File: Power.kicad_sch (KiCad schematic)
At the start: 45 parts, among them J1 Conn_01x02, J7 Conn_01x02, J8 Conn_01x02, U3 TLV75533PDRV, U6 LMR51450FNDRR, U7 LMR51450FNDRR, U8 TPS259472LRPWR, U9 NSR0340HT1G

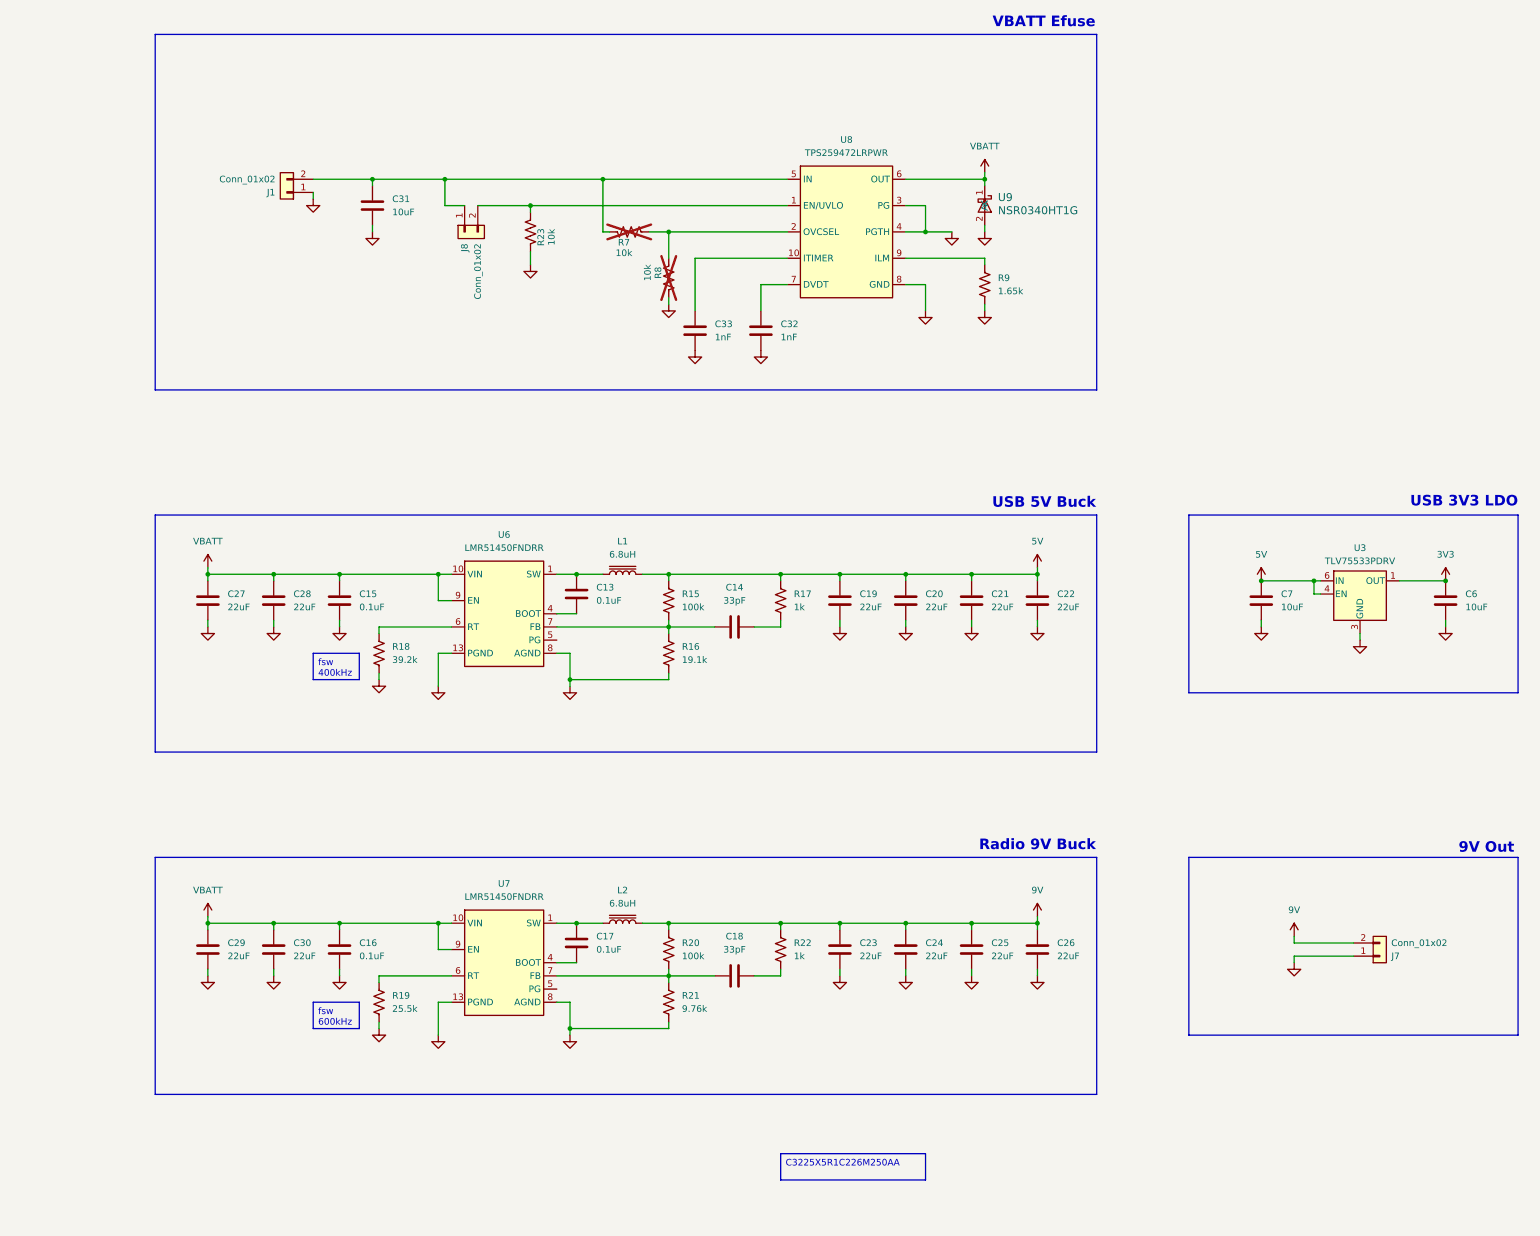
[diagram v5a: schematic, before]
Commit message: remove efuse, add led connectors
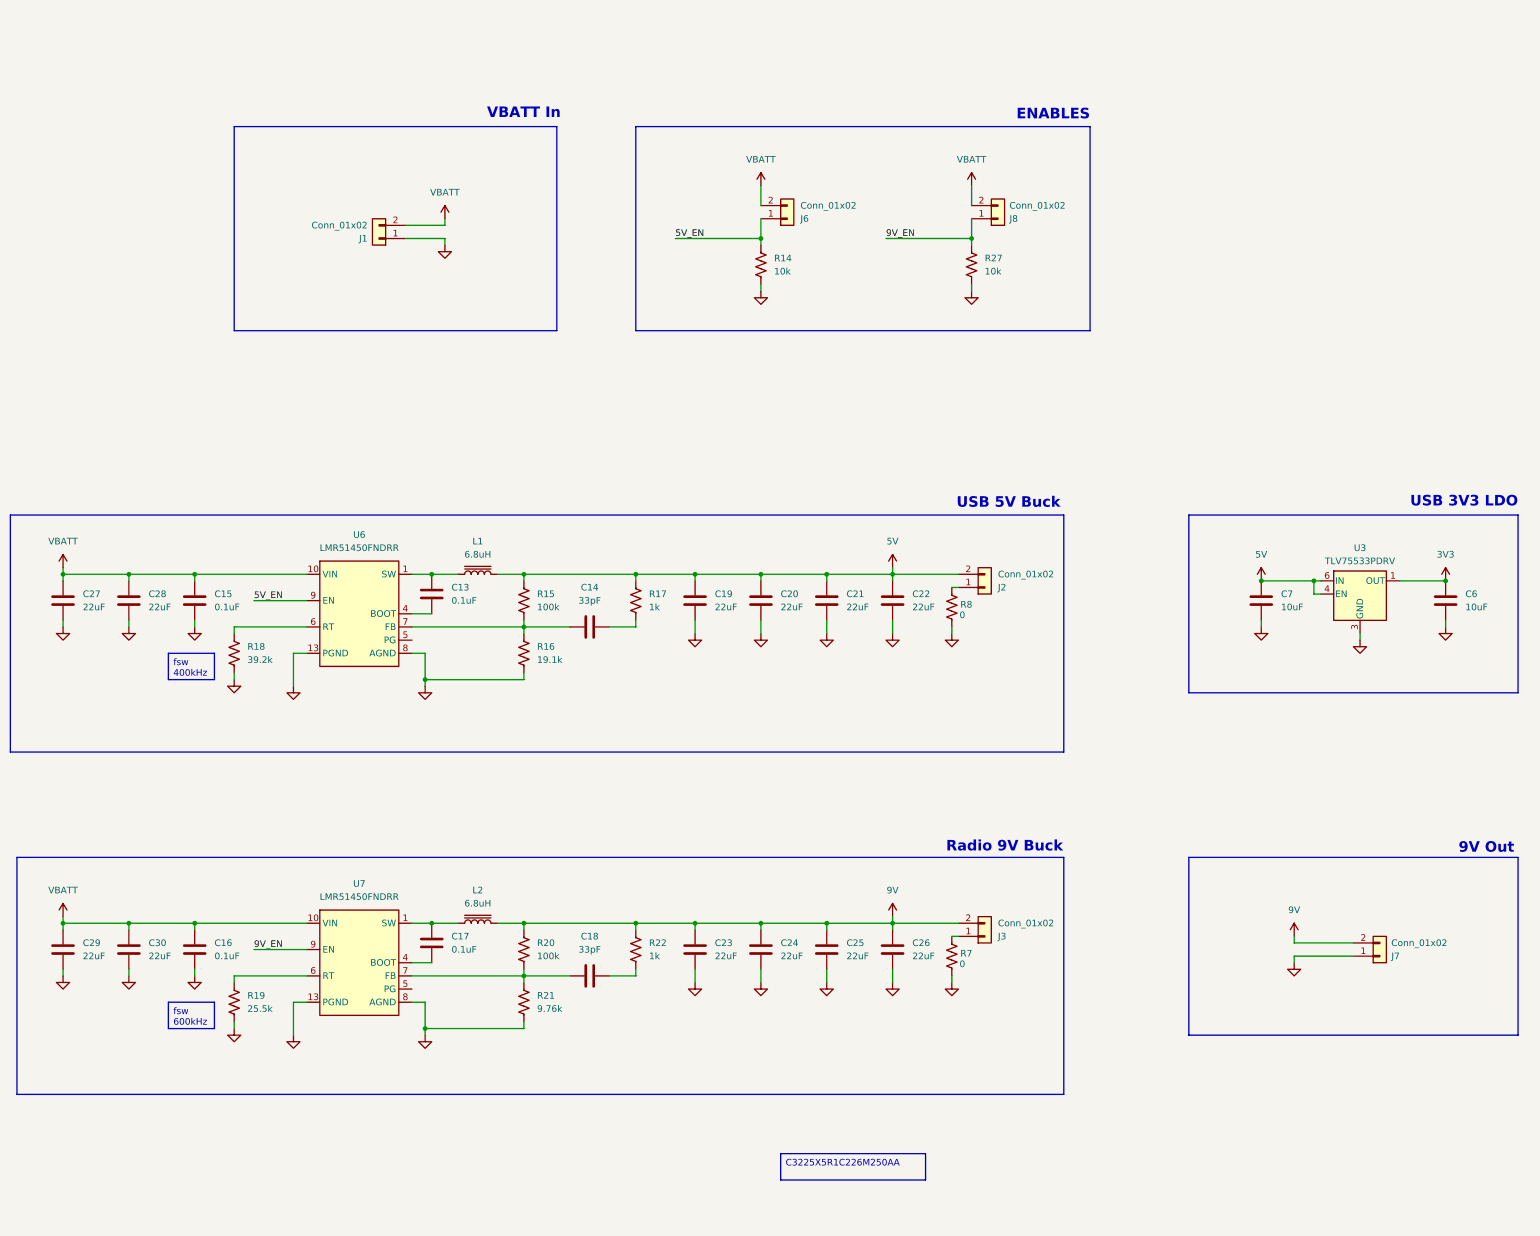
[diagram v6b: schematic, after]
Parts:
- removed C31: 10uF, Cave_Radio_PDB:R_0603_1608Metric, symbol Cave_Radio_PDB:10uF
- removed C32, C33: 1nF, Cave_Radio_PDB:C_0402_1005Metric, symbol Cave_Radio_PDB:1nF
- removed R23, R7, R8: 10k, Cave_Radio_PDB:R_0402_1005Metric, symbol Cave_Radio_PDB:10k
- removed R9: 1.65k, Cave_Radio_PDB:R_0402_1005Metric, symbol Cave_Radio_PDB:1.65k
- removed U8: TPS259472LRPWR, Cave_Radio_PDB:VQFN8_PWR_TEX, symbol Cave_Radio_PDB:TPS259472LRPWR
- removed U9: NSR0340HT1G, Cave_Radio_PDB:SOD-323_1P8X1P35_ONS, symbol Cave_Radio_PDB:NSR0340HT1G
- added J2, J3, J6: Conn_01x02, Cave_Radio_PDB:CONN_TSW-102-S_SAI, symbol Cave_Radio_PDB:Conn_01x02
- added R14, R27: 10k, Cave_Radio_PDB:R_0402_1005Metric, symbol Cave_Radio_PDB:10k
- added R7, R8: 0, Cave_Radio_PDB:R_0402_1005Metric, symbol Cave_Radio_PDB:0
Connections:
- net 5V: now also J2.2 (Pin_2)
- net 9V: now also J3.2 (Pin_2)
- net GND: now also R14.2, R27.2, R7.1, R8.1
- net VBATT: now also J1.2 (Pin_2), J8.2 (Pin_2), J6.2 (Pin_2); no longer U6.9 (EN), U7.9 (EN)
- net 9V_EN: now reaches J8.1 (Pin_1)
- net 9V_EN: now also U7.9 (EN), R27.1; no longer J1.2 (Pin_2)
- new net: J2.1 (Pin_1), R8.2
- new net: J3.1 (Pin_1), R7.2
- new net 5V_EN: J6.1 (Pin_1), R14.1, U6.9 (EN)
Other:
- note added: "ENABLES"
- note added: "VBATT In"
- note removed: "VBATT Efuse"
- moved on the sheet: C13, C14, C15, C16, C17, C18, C19, C20, C21, C22, C23, C24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
